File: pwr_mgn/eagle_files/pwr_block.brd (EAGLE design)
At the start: 100 x 80 mm, 27 parts

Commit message: more files woohoo
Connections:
- net ISET1: now also R1.2
- net ISET2: no longer R1.2
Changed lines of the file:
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@@
 <element name="JP1" library="SparkFun-Connectors" package="USB-MICROB" value="USB-MICROB" x="-26.67" y="26.67">
 <attribute name="PROD_ID" value="CONN-09505" x="0" y="0" size="1.778" layer="27" display="off"/>
+<attribute name="DESCRIPTION" value="CONN RCPT STD MICRO USB TYPE B" x="-26.67" y="26.67" size="1.778" layer="27" display="off"/>
 </element>
 <element name="C1" library="SparkFun-Capacitors" package="0603-CAP" value="1nF" x="-39.37" y="25.4">
@@
 <contactref element="U$1" pad="13"/>
 <contactref element="JP6" pad="1"/>
-<contactref element="R1" pad="2"/>
 <wire x1="-33.38" y1="27.63" x2="-27.94" y2="11.43" width="0" layer="19" extent="1-1"/>
-<wire x1="-33.44" y1="31.75" x2="-33.38" y2="27.63" width="0" layer="19" extent="1-1"/>
 </signal>
 <signal name="ISET1">
 <contactref element="U$1" pad="12"/>
 <contactref element="JP6" pad="2"/>
+<contactref element="R1" pad="2"/>
 <wire x1="-32.88" y1="27.63" x2="-25.4" y2="11.43" width="0" layer="19" extent="1-1"/>
+<wire x1="-33.44" y1="31.75" x2="-32.88" y2="27.63" width="0" layer="19" extent="1-1"/>
 </signal>
 <signal name="BATT_IN">

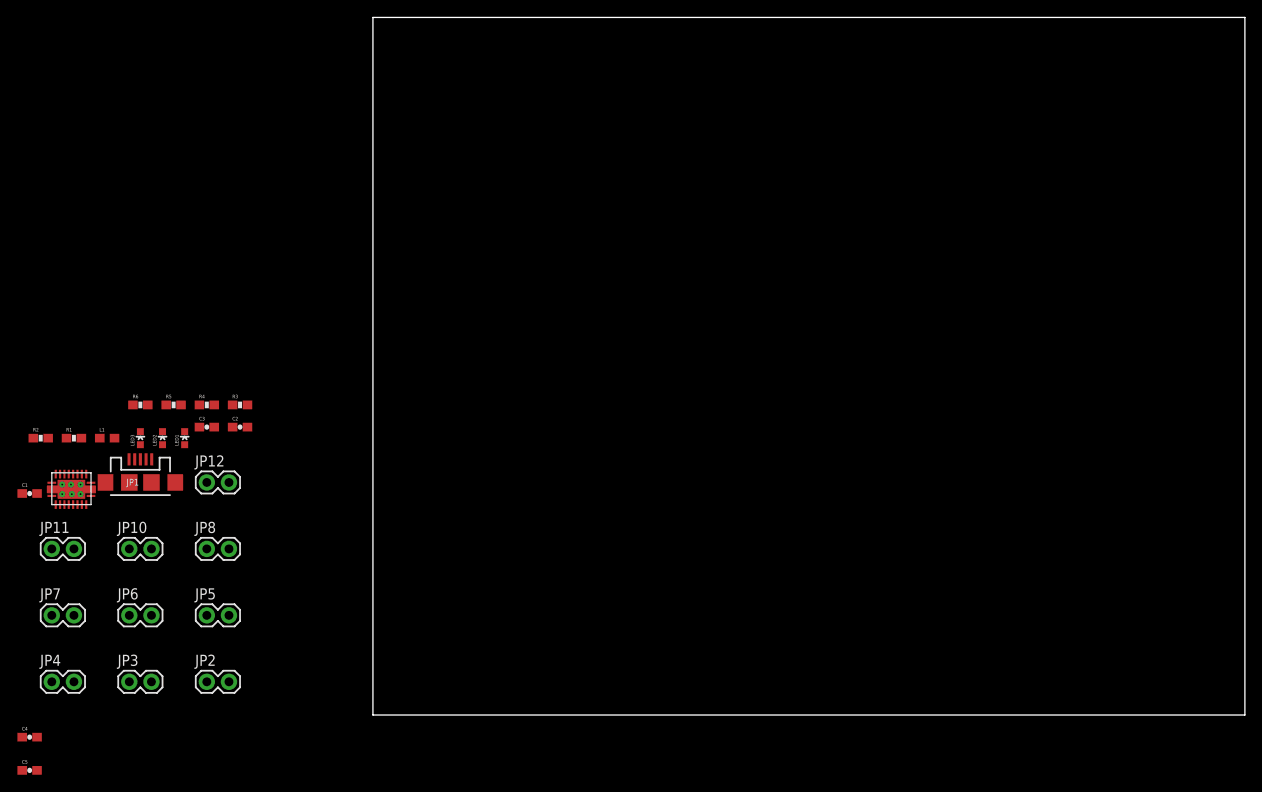
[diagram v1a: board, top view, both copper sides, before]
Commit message: routed and sent out to fab for prototype
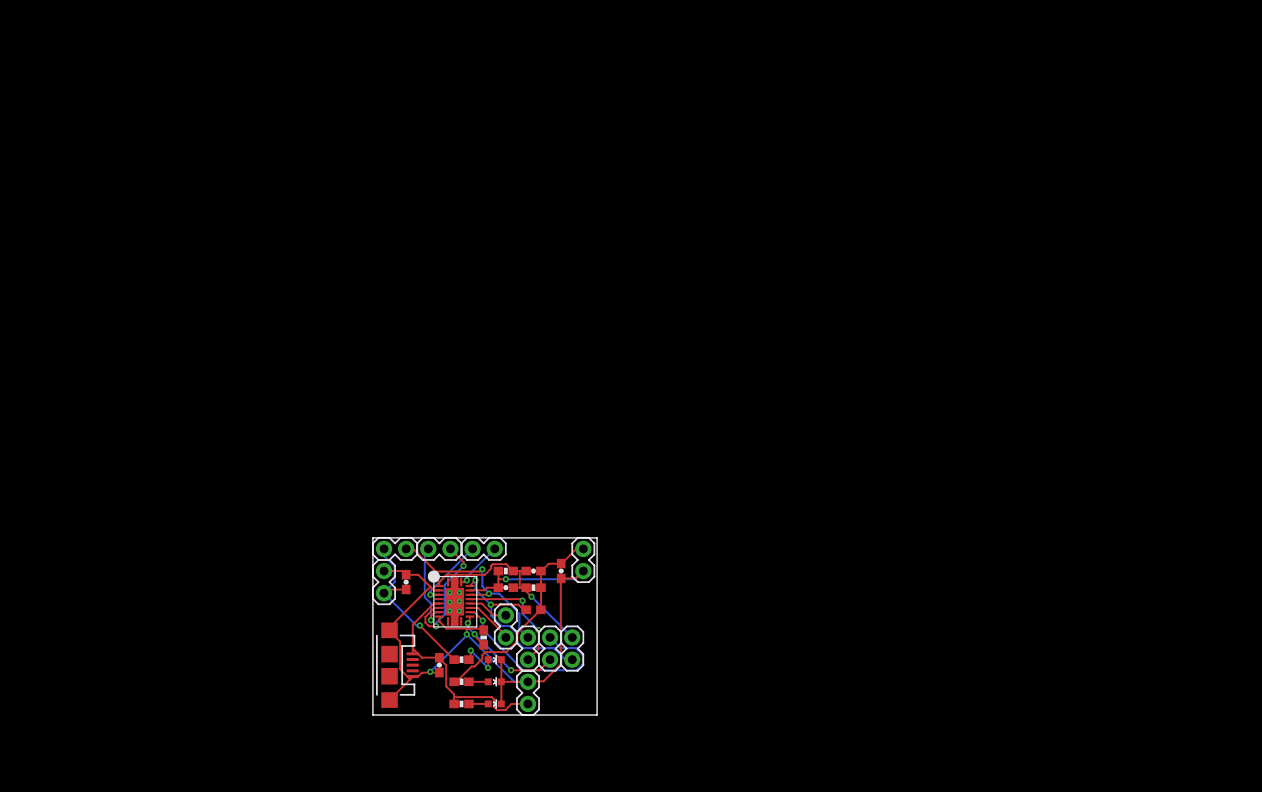
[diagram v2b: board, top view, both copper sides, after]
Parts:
- moved C5 65.1 mm to (21.6, 16.5), turned to 270 degrees
- moved R2 59.1 mm to (18.4, 14.6)
- moved C4 57.2 mm to (15.2, 14.6), turned to 180 degrees
- moved L1 52.7 mm to (18.4, 12.1)
- moved R1 52.3 mm to (12.7, 8.89), turned to 270 degrees
- moved JP7 52.1 mm to (15.2, 8.89), turned to 90 degrees
- moved C1 50.9 mm to (7.62, 5.71), turned to 270 degrees
- moved JP6 48.3 mm to (20.3, 8.89), turned to 270 degrees
- moved LED3 47.9 mm to (14.0, 6.35), turned to 270 degrees
- moved LED2 47.2 mm to (14.0, 3.81), turned to 270 degrees
- moved R6 47.0 mm to (10.2, 6.35), turned to 180 degrees
- moved LED1 46.8 mm to (14.0, 1.27), turned to 270 degrees
- moved JP3 46.0 mm to (17.8, 8.89), turned to 270 degrees
- moved R5 45.8 mm to (10.2, 3.81), turned to 180 degrees
- moved JP4 45.8 mm to (6.35, 19.1)
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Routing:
- net GND: track 0.00 -> 90.9 mm, vias 0 -> 3
- net USB_PWR: track 0.00 -> 26.7 mm
- net VOUT: track 0.00 -> 24.5 mm
- net FB: track 0.00 -> 23.4 mm, vias 0 -> 1
- net BATT_IN: track 0.00 -> 22.8 mm, vias 0 -> 2
- net ISET2: track 0.00 -> 22.2 mm, vias 0 -> 1
- net SW: track 0.00 -> 21.9 mm, vias 0 -> 2
- net BATT: track 0.00 -> 20.0 mm, vias 0 -> 1
- net ISET1: track 0.00 -> 15.0 mm, vias 0 -> 3
- net STAT1: track 0.00 -> 14.9 mm, vias 0 -> 2
- net BATT_OUT: track 0.00 -> 14.1 mm, vias 0 -> 2
- net STAT2: track 0.00 -> 10.3 mm, vias 0 -> 1
- net EN: track 0.00 -> 8.31 mm, vias 0 -> 1
- net FPWM: track 0.00 -> 5.67 mm, vias 0 -> 1
- net PG: track 0.00 -> 5.66 mm
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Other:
- board size 100 x 80 mm -> 25.7 x 20.3 mm
